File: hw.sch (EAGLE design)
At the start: 75 parts, among them IC1 ATMEGA32U4-AU, IC2 LTC485S, IC3 MCP16301/H, IC5 DS18S20, J1 Temperature sensor, J2 Flow sensor, J3 Level sensor, Q1 GSX-533, SW1 SPS, SW2 SPS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

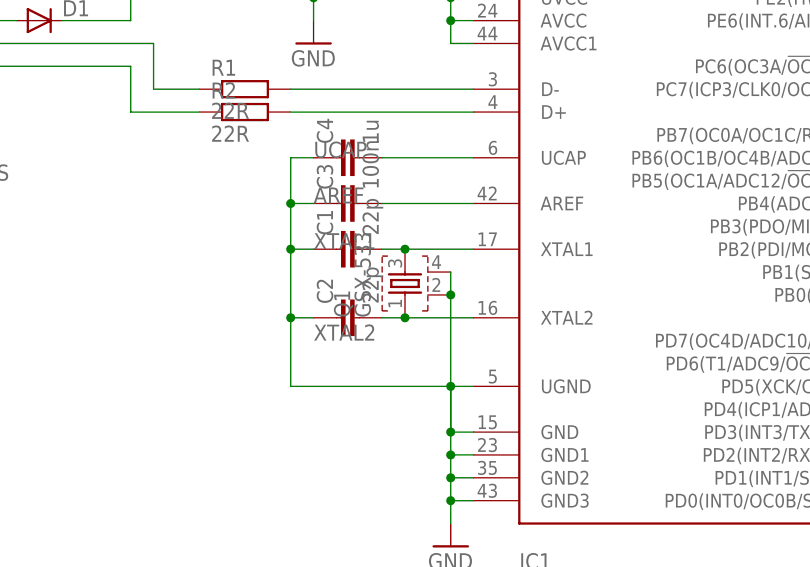
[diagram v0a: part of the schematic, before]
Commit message: Changed library of crystal
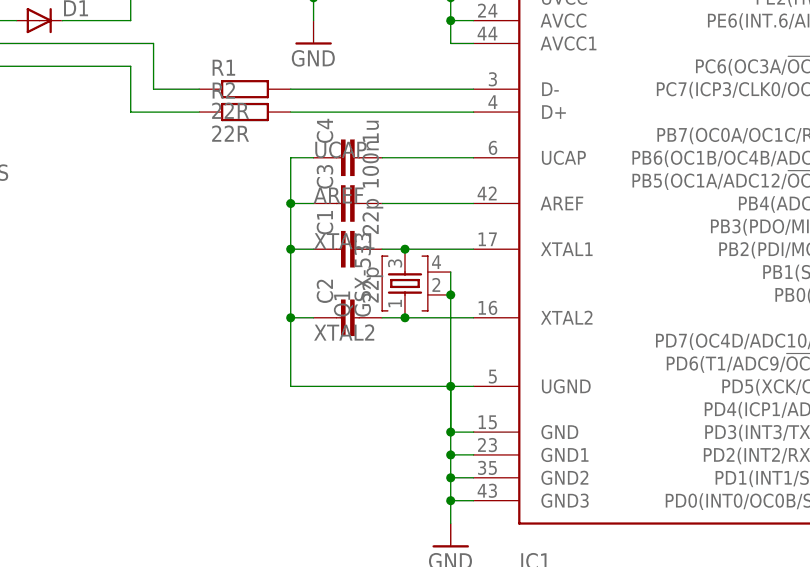
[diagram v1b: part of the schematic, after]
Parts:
- Q1: device GSX-533:GSX-533 -> crystal-golledge:GSX-533
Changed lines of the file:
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@@
 <part name="P+20" library="supply1" deviceset="+5V" device=""/>
 <part name="GND18" library="supply1" deviceset="GND" device=""/>
-<part name="Q1" library="GSX-533" deviceset="GSX-533" device=""/>
+<part name="Q1" library="crystal-golledge" library_urn="urn:adsk.eagle:library:4881003" deviceset="GSX-533" device="" package3d_urn="urn:adsk.eagle:package:4881006/2"/>
 </parts>
 <sheets>
